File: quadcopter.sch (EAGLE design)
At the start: 65 parts, among them J1 ISP, M1 MOTOR_PADS, M2 MOTOR_PADS, M3 MOTOR_PADS, M4 MOTOR_PADS, U1 ATMEGA128RFA1

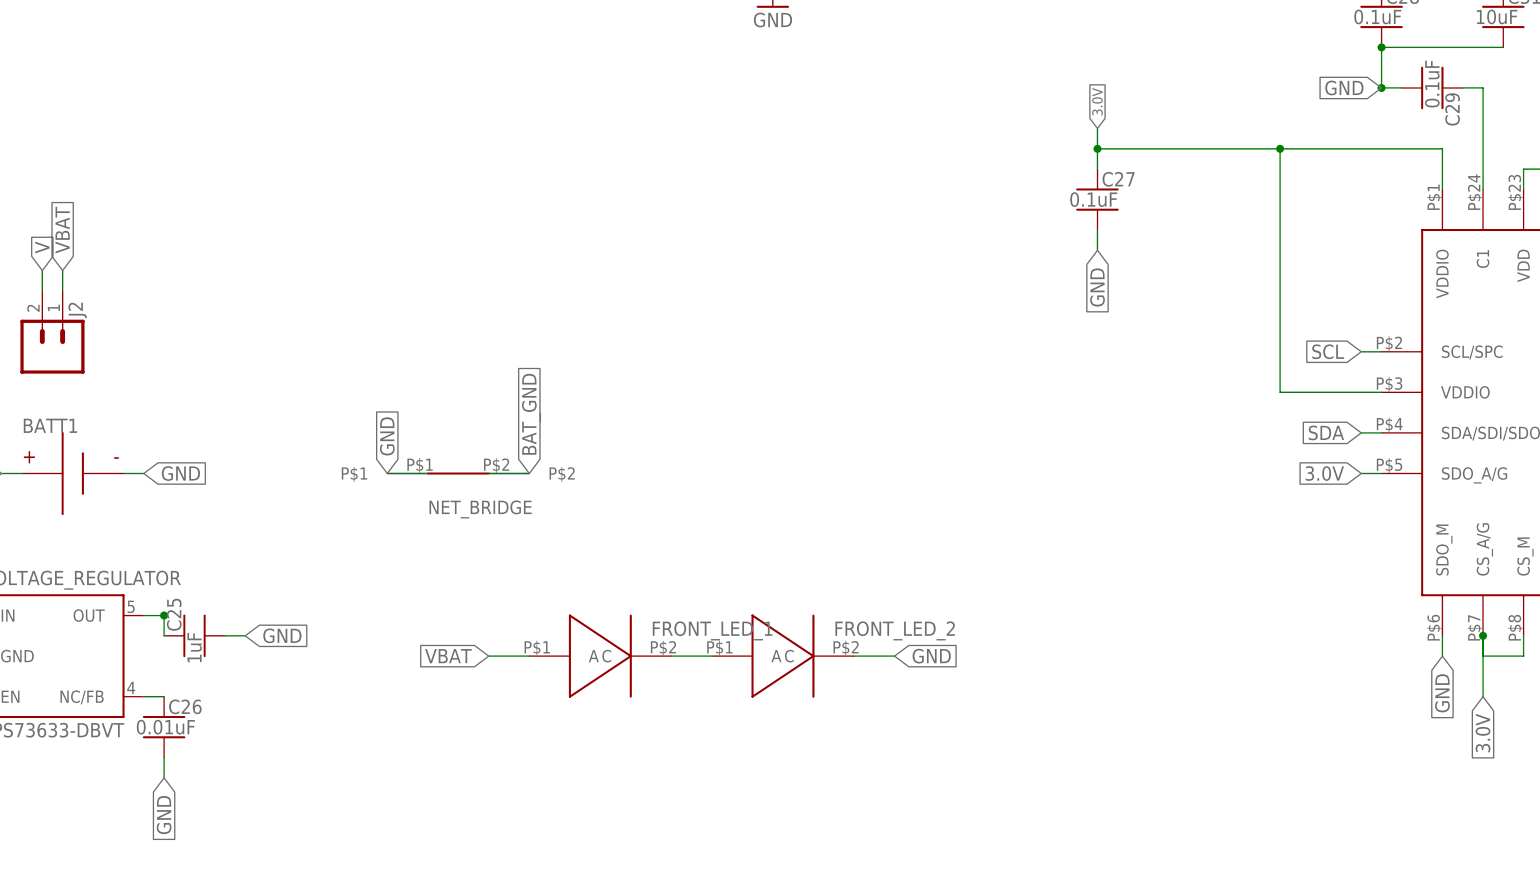
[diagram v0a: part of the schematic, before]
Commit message: Added pull up resistors, fixed leds
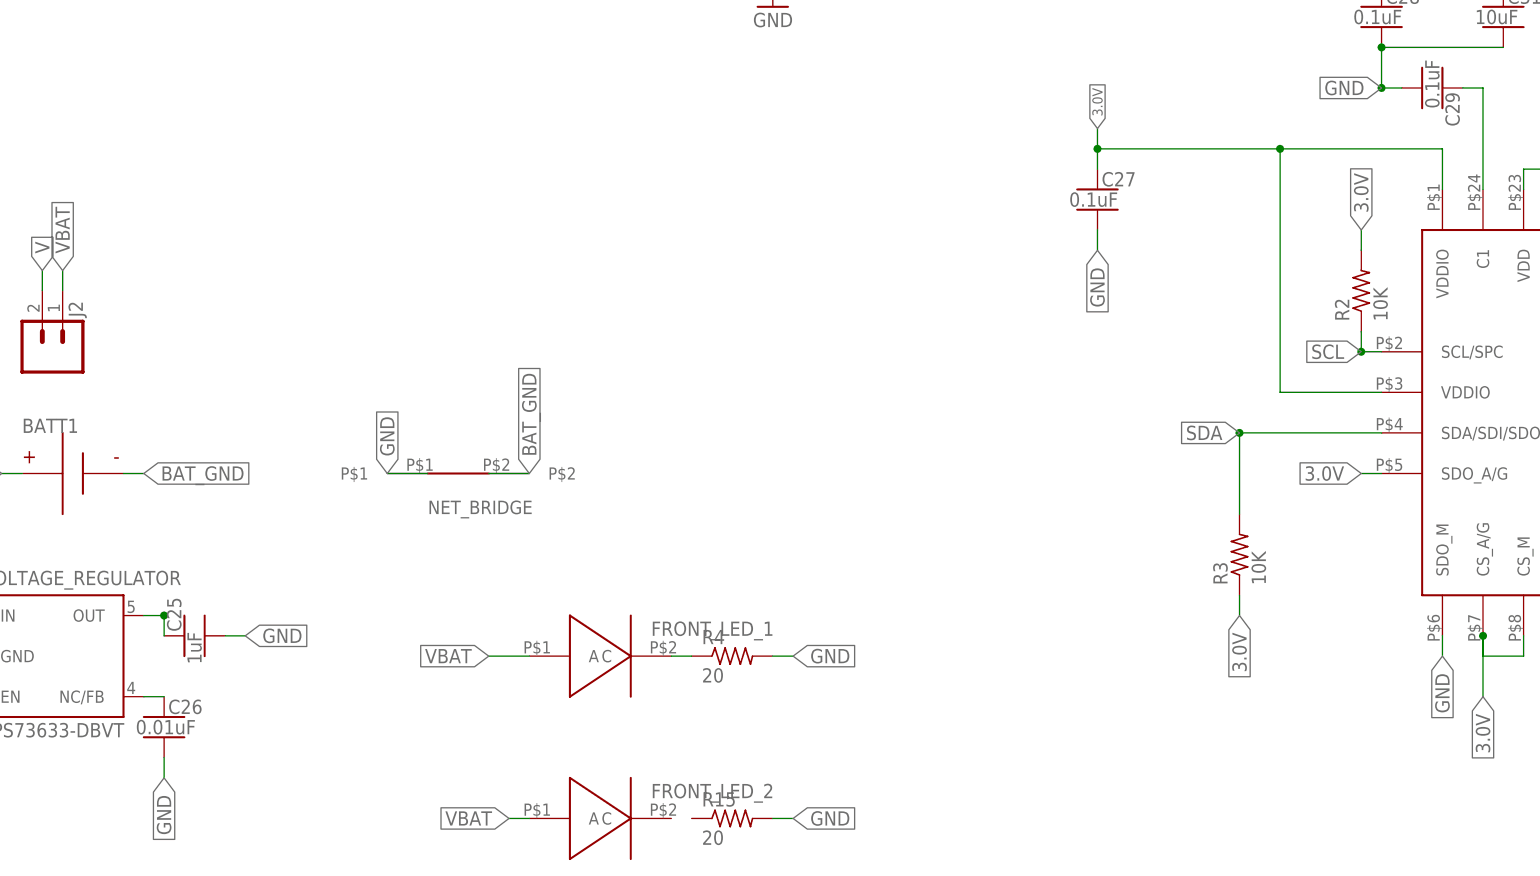
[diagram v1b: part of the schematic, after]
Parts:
- added R15, R4: 20, quadparts_prebuilt:RESISTOR_SMD-2012-0805-20
- added R2, R3: 10K, quadparts_prebuilt:RESISTOR_SMD-2012-0805-10K
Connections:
- removed net N$5: FRONT_LED_1.C, FRONT_LED_2.A
- new net N$1: FRONT_LED_1.C, R4.1
- net 3.0V: now also R2.2, R3.1
- net BAT_GND: now also BATT1.N
- net GND: now also R15.2, R4.2; no longer BATT1.N, FRONT_LED_2.C
- net SCL: now also R2.1
- net SDA: now also R3.2
- net VBAT: now also FRONT_LED_2.A
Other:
- moved on the sheet: FRONT_LED_2
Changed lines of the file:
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@@
 <part name="FRONT_LED_1" library="LEDs" deviceset="LED" device="-0805-GREEN"/>
 <part name="FRONT_LED_2" library="LEDs" deviceset="LED" device="-0805-GREEN"/>
+<part name="R2" library="quadparts_prebuilt" deviceset="RESISTOR_" device="SMD-2012-0805-10K" value="10K"/>
+<part name="R3" library="quadparts_prebuilt" deviceset="RESISTOR_" device="SMD-2012-0805-10K" value="10K"/>
+<part name="R4" library="quadparts_prebuilt" deviceset="RESISTOR_" device="SMD-2012-0805-20" value="20"/>
+<part name="R15" library="quadparts_prebuilt" deviceset="RESISTOR_" device="SMD-2012-0805-20" value="20"/>
 </parts>
 <sheets>
@@
 <instance part="J3" gate="G$1" x="287.02" y="-40.64"/>
 <instance part="FRONT_LED_1" gate="G$1" x="71.12" y="-76.2"/>
-<instance part="FRONT_LED_2" gate="G$1" x="93.98" y="-76.2"/>
+<instance part="FRONT_LED_2" gate="G$1" x="71.12" y="-96.52"/>
+<instance part="R2" gate="G$1" x="165.1" y="-30.48" rot="R90"/>
+<instance part="R3" gate="G$1" x="149.86" y="-63.5" rot="R90"/>
+<instance part="R4" gate="G$1" x="86.36" y="-76.2"/>
+<instance part="R15" gate="G$1" x="86.36" y="-96.52"/>
 </instances>
 <busses>
@@
 <wire x1="180.34" y1="119.38" x2="190.5" y2="119.38" width="0.1524" layer="91"/>
 <label x="190.5" y="119.38" size="1.27" layer="95" xref="yes"/>
-</segment>
-<segment>
-<pinref part="BATT1" gate="G$1" pin="N"/>
-<wire x1="10.16" y1="-53.34" x2="12.7" y2="-53.34" width="0.1524" layer="91"/>
-<label x="12.7" y="-53.34" size="1.778" layer="95" xref="yes"/>
 </segment>
 <segment>
@@
 </segment>
 <segment>
-<pinref part="FRONT_LED_2" gate="G$1" pin="C"/>
-<wire x1="101.6" y1="-76.2" x2="106.68" y2="-76.2" width="0.1524" layer="91"/>
-<label x="106.68" y="-76.2" size="1.778" layer="95" xref="yes"/>
+<pinref part="R15" gate="G$1" pin="2"/>
+<wire x1="91.44" y1="-96.52" x2="93.98" y2="-96.52" width="0.1524" layer="91"/>
+<label x="93.98" y="-96.52" size="1.778" layer="95" xref="yes"/>
+</segment>
+<segment>
+<pinref part="R4" gate="G$1" pin="2"/>
+<wire x1="91.44" y1="-76.2" x2="93.98" y2="-76.2" width="0.1524" layer="91"/>
+<label x="93.98" y="-76.2" size="1.778" layer="95" xref="yes"/>
 </segment>
 </net>
@@
 <segment>
 <pinref part="U$5" gate="G$1" pin="SDA/SDI/SDO"/>
-<wire x1="167.64" y1="-48.26" x2="165.1" y2="-48.26" width="0.1524" layer="91"/>
-<label x="165.1" y="-48.26" size="1.778" layer="95" rot="R180" xref="yes"/>
+<pinref part="R3" gate="G$1" pin="2"/>
+<wire x1="167.64" y1="-48.26" x2="149.86" y2="-48.26" width="0.1524" layer="91"/>
+<wire x1="149.86" y1="-48.26" x2="149.86" y2="-58.42" width="0.1524" layer="91"/>
+<junction x="149.86" y="-48.26"/>
+<label x="149.86" y="-48.26" size="1.778" layer="95" rot="R180" xref="yes"/>
 </segment>
 </net>
@@
 <wire x1="167.64" y1="-38.1" x2="165.1" y2="-38.1" width="0.1524" layer="91"/>
 <label x="165.1" y="-38.1" size="1.778" layer="95" rot="R180" xref="yes"/>
+<junction x="165.1" y="-38.1"/>
+<pinref part="R2" gate="G$1" pin="1"/>
+<wire x1="165.1" y1="-38.1" x2="165.1" y2="-35.56" width="0.1524" layer="91"/>
 </segment>
 </net>
@@
 <wire x1="60.96" y1="-76.2" x2="55.88" y2="-76.2" width="0.1524" layer="91"/>
 <label x="55.88" y="-76.2" size="1.778" layer="95" rot="R180" xref="yes"/>
+</segment>
+<segment>
+<pinref part="FRONT_LED_2" gate="G$1" pin="A"/>
+<wire x1="60.96" y1="-96.52" x2="58.42" y2="-96.52" width="0.1524" layer="91"/>
+<label x="58.42" y="-96.52" size="1.778" layer="95" rot="R180" xref="yes"/>
 </segment>
 </net>
@@
 <label x="165.1" y="-53.34" size="1.778" layer="95" rot="R180" xref="yes"/>
 </segment>
+<segment>
+<pinref part="R3" gate="G$1" pin="1"/>
+<wire x1="149.86" y1="-68.58" x2="149.86" y2="-71.12" width="0.1524" layer="91"/>
+<label x="149.86" y="-71.12" size="1.778" layer="95" rot="R270" xref="yes"/>
+</segment>
+<segment>
+<pinref part="R2" gate="G$1" pin="2"/>
+<wire x1="165.1" y1="-25.4" x2="165.1" y2="-22.86" width="0.1524" layer="91"/>
+<label x="165.1" y="-22.86" size="1.778" layer="95" rot="R90" xref="yes"/>
+</segment>
 </net>
 <net name="N$18" class="0">
@@
 <wire x1="297.18" y1="-17.78" x2="307.34" y2="-17.78" width="0.1524" layer="91"/>
 <label x="307.34" y="-17.78" size="1.27" layer="95" xref="yes"/>
+</segment>
+<segment>
+<pinref part="BATT1" gate="G$1" pin="N"/>
+<wire x1="10.16" y1="-53.34" x2="12.7" y2="-53.34" width="0.1524" layer="91"/>
+<label x="12.7" y="-53.34" size="1.778" layer="95" xref="yes"/>
 </segment>
 </net>
@@
 </segment>
 </net>
-<net name="N$5" class="0">
+<net name="N$1" class="0">
 <segment>
 <pinref part="FRONT_LED_1" gate="G$1" pin="C"/>
-<pinref part="FRONT_LED_2" gate="G$1" pin="A"/>
-<wire x1="78.74" y1="-76.2" x2="83.82" y2="-76.2" width="0.1524" layer="91"/>
-</segment>
-</net>
+<pinref part="R4" gate="G$1" pin="1"/>
+<wire x1="78.74" y1="-76.2" x2="81.28" y2="-76.2" width="0.1524" layer="91"/>
+</segment>
+</net>

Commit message: Fix quadcopter shematic and parts in quadcopter_jay
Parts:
- removed J1: ISP, SparkFun-Connectors:AVR_SPI_PRG_6NS
- removed JP1, JP9: FTDI, SparkFun-Connectors:FTDI_BASICPTH
- added J4: AVR_SPI_PRG_6NS, quadparts_prebuilt:AVR_SPI_PRG_6NS
- added JP2, JP3: FTDI_BASICPTH, quadparts_prebuilt:FTDI_BASICPTH
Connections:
- net DTR: no longer JP9.1
- net FILTERED1: now also U$4.G
- net FILTERED2: now also U$2.G
- net FILTERED3: now also U$3.G
- net FILTERED4: now also U$1.G
- net GND: now also J4.6; no longer J1.6, JP9.6
- net MISO: now also J4.1; no longer J1.1
- net MOSI: now also J4.4; no longer J1.4
- net RESET: now also J4.5; no longer J1.5
- net RX0: no longer JP9.3
- net SCK: now also J4.3; no longer J1.3
- net TX0: no longer JP9.2
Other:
- moved on the sheet: C15, C16, C17, C18, C19, C20, C21, C22, C23, D1, D2, D3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
